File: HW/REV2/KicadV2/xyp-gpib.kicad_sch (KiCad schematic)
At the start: 25 parts, among them J1 USB_C_Receptacle_USB2.0, SW1 SW_Push, U1 ATmega32U4-MU, Y1 CX2016DB16000D0WZRC1

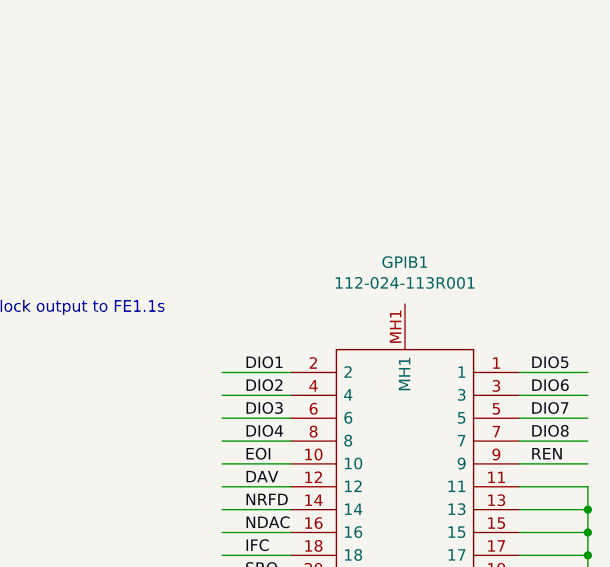
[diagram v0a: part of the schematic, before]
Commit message: Updated FW Version and release of first UsbGpib GUI version
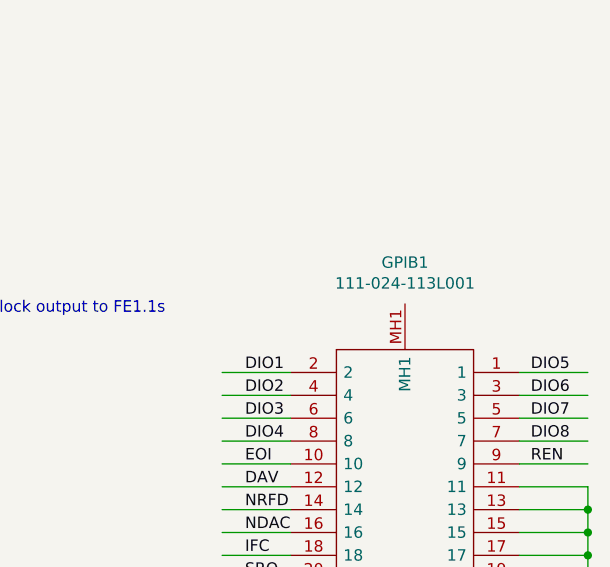
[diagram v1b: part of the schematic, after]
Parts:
- GPIB1: value 112-024-113R001 -> 111-024-113L001

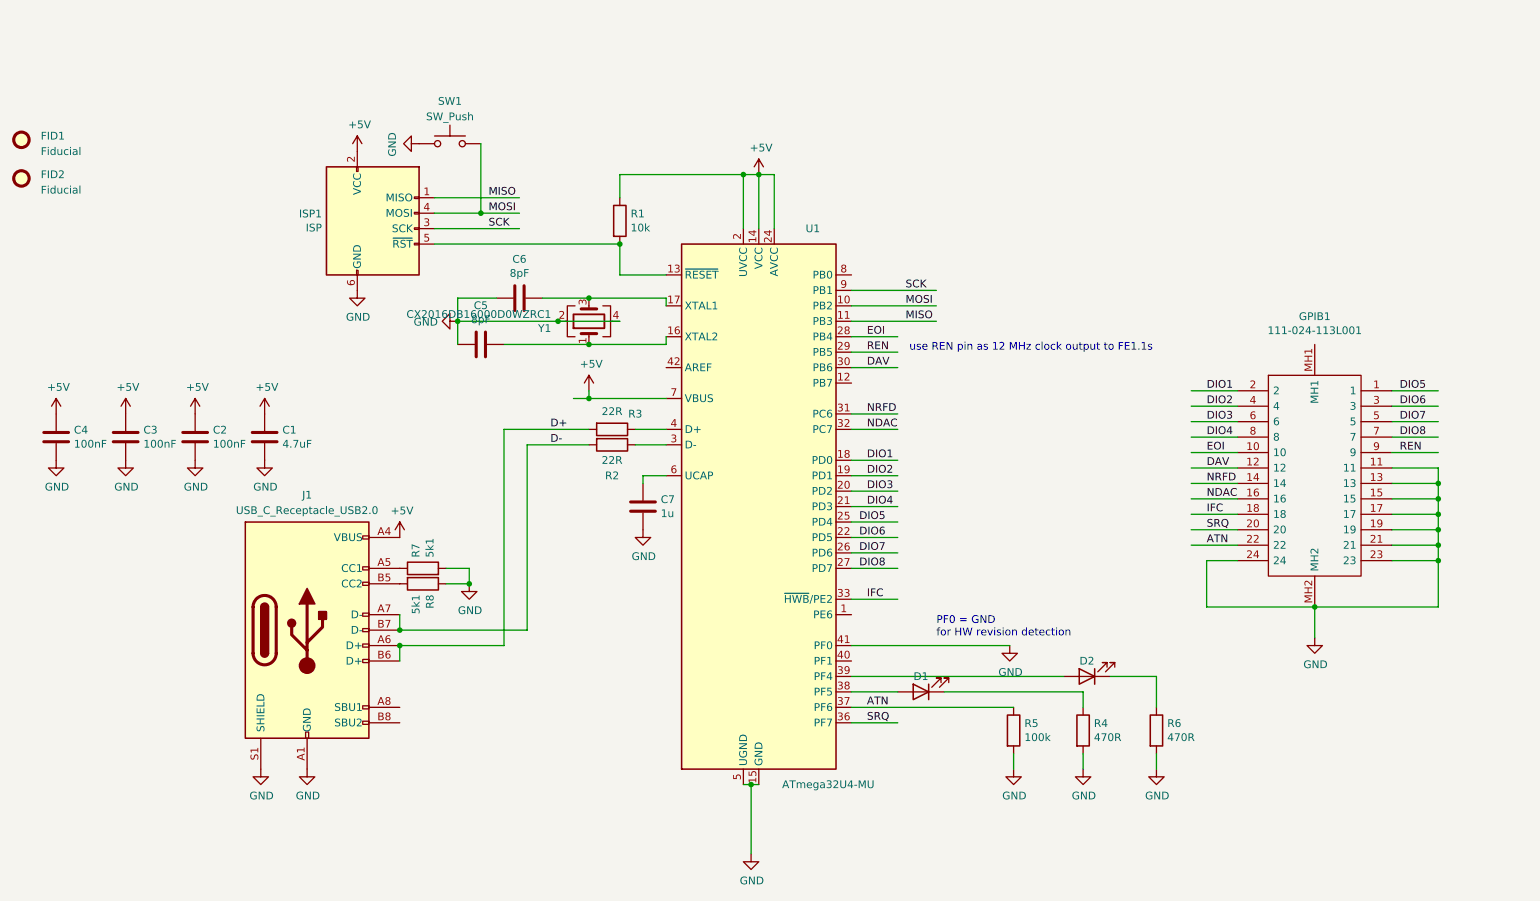
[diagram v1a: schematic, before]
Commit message: [MOD] Cleanup schematic + add USBLC6-2P6
Signed-off-by: Silvano Cortesi <silvano.cortesi@hotmail.com>
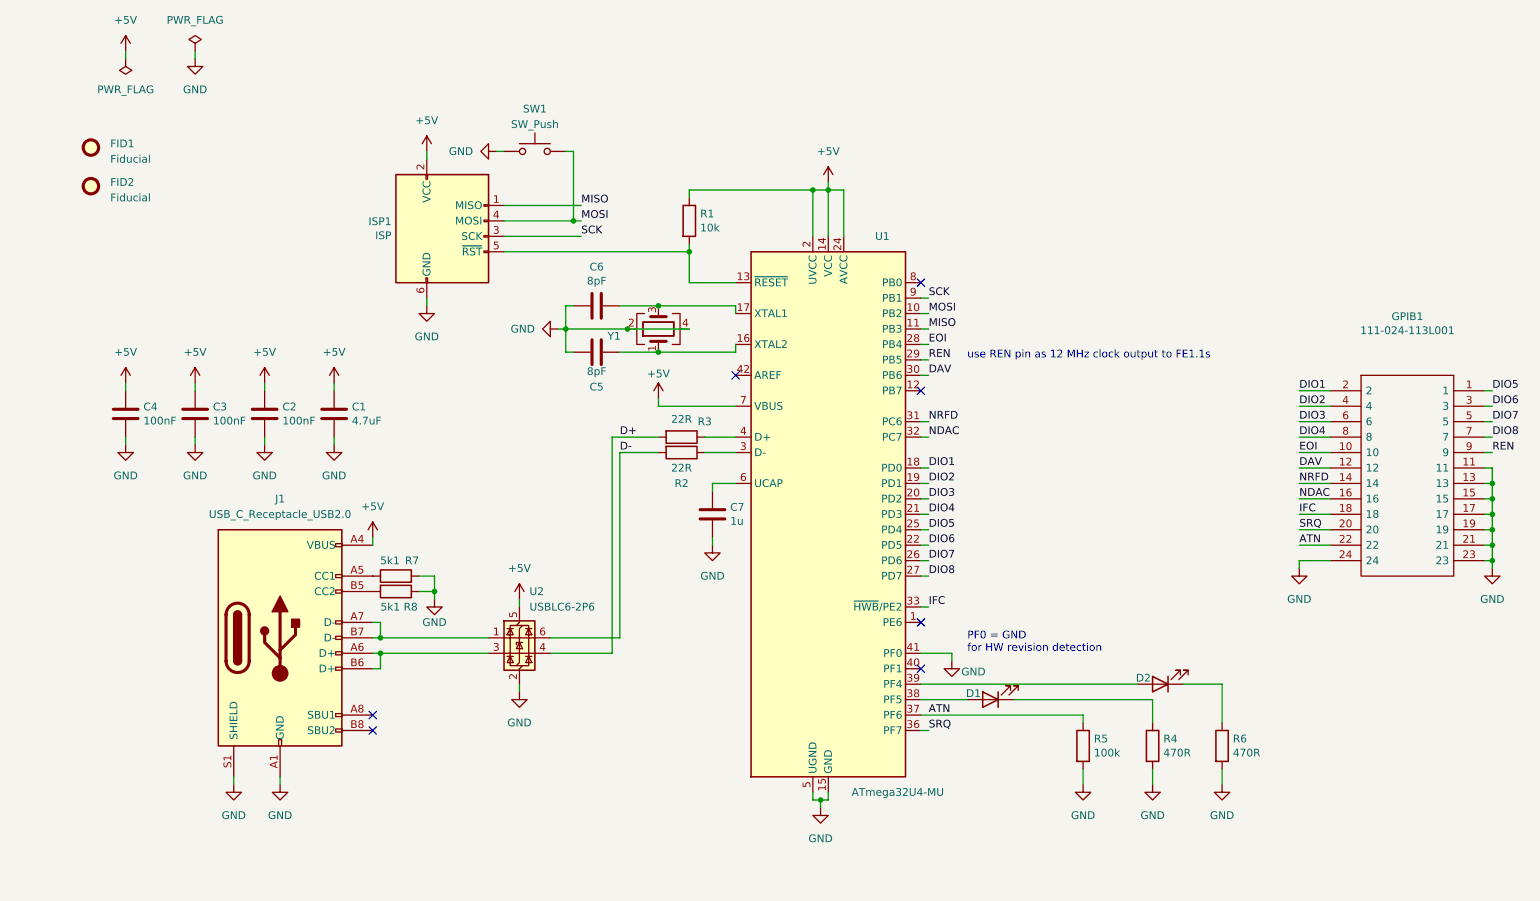
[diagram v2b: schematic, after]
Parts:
- added U2: USBLC6-2P6, Package_TO_SOT_SMD:SOT-666, symbol Power_Protection:USBLC6-2P6
- GPIB1: footprint gpib:112024113R001 -> usbgpib-footprints:GPIB; symbol conn-gpib:112-024-113R001 -> usbgpib-symbols:GPIB
- ISP1: footprint Kai:EdgeProg -> usbgpib-footprints:EdgeProg-ISP
- J1: symbol Connector:USB_C_Receptacle_USB2.0 -> Connector:USB_C_Receptacle_USB2.0_16P
- U1: symbol MCU_Microchip_ATmega:ATmega32U4-MU -> MCU_Microchip_ATmega:ATmega32U4-M
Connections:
- net +5V: now also U2.5 (VBUS)
- net D+: now also U2.4 (I/O2); no longer J1.A6 (D+), J1.B6 (D+)
- net D-: now also U2.6 (I/O1); no longer J1.A7 (D-), J1.B7 (D-)
- net GND: now also U2.2 (GND); no longer GPIB1.MH2
- new net: J1.A7 (D-), J1.B7 (D-), U2.1 (I/O1)
- new net: J1.A6 (D+), J1.B6 (D+), U2.3 (I/O2)
- no-connect marks 0 -> 7
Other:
- company: (none) -> xyphro
- title: (none) -> UsbGpib
- moved on the sheet: C1, C2, C3, C4, C5, C6, C7, FID1, FID2, ISP1, J1, R1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
